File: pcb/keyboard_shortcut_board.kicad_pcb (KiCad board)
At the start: 2 copper layers, 96.4 x 90.9 mm, 34 parts, among them SW1 SW_Push, SW10 RotaryEncoder, SW2 SW_Push, SW3 SW_Push, SW4 SW_Push, SW5 SW_Push, SW6 SW_Push, SW7 SW_Push, SW8 SW_Push, SW9 SW_Push, U1 MOUDLE-SEEEDUINO-XIAO, U2 ER_OLEDM0.91_1x-I2C

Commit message: fix schematic power rails
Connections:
- net Net-(D1-VSS) renamed GND
- D1 pad 1: Net-(D1-VDD) -> +5V
- D2 pad 1: Net-(D1-VDD) -> +5V
- D3 pad 1: Net-(D1-VDD) -> +5V
- D4 pad 1: Net-(D1-VDD) -> +5V
- D5 pad 1: Net-(D1-VDD) -> +5V
- D6 pad 1: Net-(D1-VDD) -> +5V
- D7 pad 1: Net-(D1-VDD) -> +5V
- D8 pad 1: Net-(D1-VDD) -> +5V
- D9 pad 1: Net-(D1-VDD) -> +5V
- U1 pad 12: Net-(D1-VDD) -> unconnected-(U1-3V3-Pad12)
- U1 pad 14: Net-(U1-5V) -> +5V
- U2 pad 2: Net-(U1-5V) -> +5V
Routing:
- net +5V: track 0.00 -> 262.0 mm, vias 0 -> 4
- net Net-(D1-VDD): track 197.5 -> 0.00 mm, vias 3 -> 0
- net Net-(U1-5V): track 136.1 -> 0.00 mm, vias 7 -> 0
- net GND: track 257.2 -> 275.9 mm, vias 9 -> 16

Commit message: move XIAO 5mm right so USB-C clears the case wall
Receptacle sat 7.64mm inboard of the right board edge after the mounting
margin was added, too deep for a USB-C plug overmold to reach. Now 2.64mm.

Re-routed all 13 nets on the XIAO. Also repointed the SK6812 footprints at
the 3D model that actually ships with KiCad. DRC unchanged: 0 unconnected,
44 LED slot-clearance errors inherent to the supplied footprint.
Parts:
- moved U1 5.00 mm to (115.5, 94.7)
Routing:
- net Net-(U1-PA8_A4_D4_SDA): track 118.5 -> 108.8 mm, vias 4 -> 2
- net Net-(U1-PA9_A5_D5_SCL): track 113.9 -> 104.3 mm, vias 6 -> 2
- net Net-(U1-PA6_A10_D10_MOSI): track 61.7 -> 68.1 mm, vias 1 -> 0
- net Net-(U1-PA5_A9_D9_MISO): track 72.0 -> 65.7 mm, vias 4 -> 2
- net Net-(U1-PA7_A8_D8_SCK): track 55.2 -> 60.6 mm, vias 3 -> 1
- net Net-(D16-K): track 45.5 -> 40.9 mm
- net Net-(D1-DIN): track 70.4 -> 74.7 mm
- net Net-(U1-PB09_A7_D7_RX): track 62.2 -> 64.8 mm, vias 8 -> 5
- net +5V: track 262.0 -> 259.6 mm, vias 4 -> 18
- net Net-(D13-K): track 67.8 -> 69.9 mm
- net Net-(D10-K): track 80.2 -> 82.3 mm
- net Net-(U1-PA11_A3_D3): track 97.5 -> 99.6 mm, vias 4 -> 1
- net GND: track 275.9 -> 274.9 mm

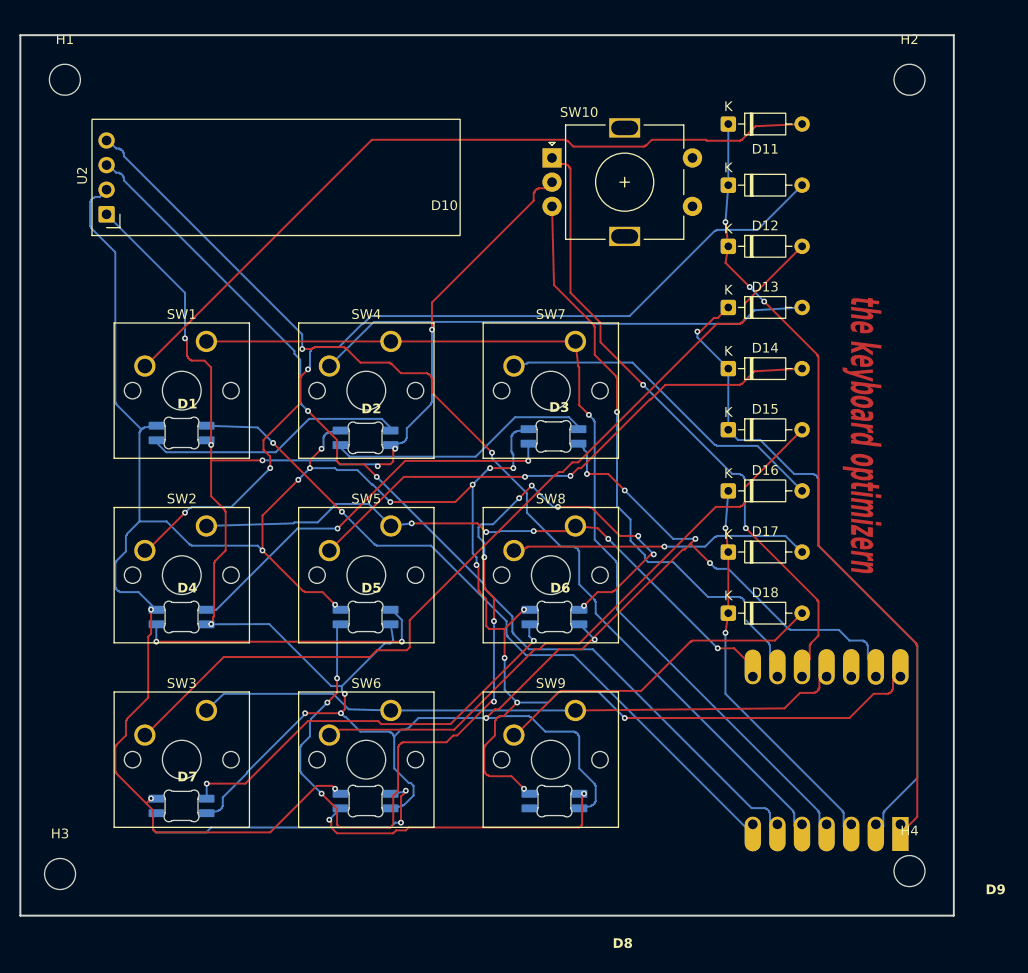
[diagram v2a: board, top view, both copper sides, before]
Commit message: square up the M3 mounting holes and add the board STEP
Holes were off a symmetric pattern by up to 0.7mm, so the case could not use
a rectangular pattern. Now a true 88.226 x 82.748 rectangle, 4.076mm inset on
all four edges.

That inset centres the bottom-right hole in the 8.15mm band between the XIAO
and the board edge, raising its clearance from 3.55 to 4.08mm so the heatset
boss can be 8.15mm OD instead of 7.1mm.

DRC unchanged: 0 unconnected, 44 LED slot-clearance errors from the supplied
SK6812 footprint. Gerbers and STEP regenerated and verified against the board.
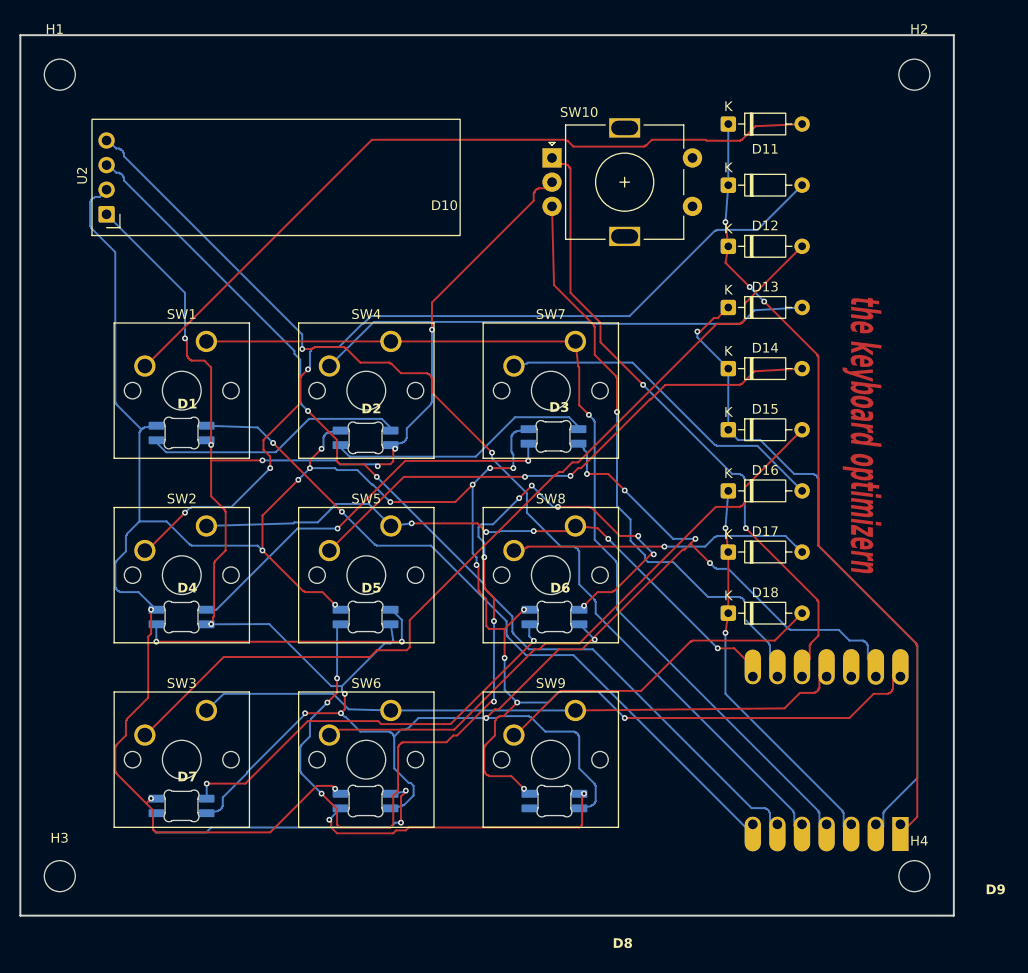
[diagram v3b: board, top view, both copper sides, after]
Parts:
- moved H1 0.74 mm to (36.3, 25.0)
- moved H2 0.73 mm to (124.5, 25.0)
- moved H4 0.73 mm to (124.5, 107.7)
- moved H3 0.23 mm to (36.3, 107.7)
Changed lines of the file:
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@@
 	(footprint "MountingHole:MountingHole_3.2mm_M3"
 		(layer "F.Cu")
-		(at 124.0172 25.4768)
+		(at 124.5186 24.9528)
 		(property "Reference" "H2"
-			(at 0 -4.15 0)
+			(at 0.5014 -4.6740 0)
 			(layer "F.SilkS")
 			(effects
@@
 		)
 		(property "Value" "MountingHole_3.2mm_M3"
-			(at 0 4.15 0)
+			(at 0.5014 3.6260 0)
 			(layer "F.Fab")
 			(effects
@@
 		)
 		(property "Datasheet" ""
-			(at 0 0 0)
+			(at 0.5014 -0.5240 0)
 			(layer "F.Fab")
 			(hide yes)
@@
 		)
 		(property "Description" ""
-			(at 0 0 0)
+			(at 0.5014 -0.5240 0)
 			(layer "F.Fab")
 			(hide yes)
@@
 		)
 		(property "KiLib_Generator" "mounting_hardware/mounting_hole"
-			(at 0 0 0)
+			(at 0.5014 -0.5240 0)
 			(layer "F.SilkS")
 			(hide yes)
@@
 		)
 		(fp_text user "${REFERENCE}"
-			(at 0 0 0)
+			(at 0.5014 -0.5240 0)
 			(layer "F.Fab")
 			(effects
@@
 	(footprint "MountingHole:MountingHole_3.2mm_M3"
 		(layer "F.Cu")
-		(at 124.0172 107.1768)
+		(at 124.5186 107.7007)
 		(property "Reference" "H4"
-			(at 0 -4.15 0)
+			(at 0.5014 -3.6261 0)
 			(layer "F.SilkS")
 			(effects
@@
 		)
 		(property "Value" "MountingHole_3.2mm_M3"
-			(at 0 4.15 0)
+			(at 0.5014 4.6739 0)
 			(layer "F.Fab")
 			(effects
@@
 		)
 		(property "Datasheet" ""
-			(at 0 0 0)
+			(at 0.5014 0.5239 0)
 			(layer "F.Fab")
 			(hide yes)
@@
 		)
 		(property "Description" ""
-			(at 0 0 0)
+			(at 0.5014 0.5239 0)
 			(layer "F.Fab")
 			(hide yes)
@@
 		)
 		(property "KiLib_Generator" "mounting_hardware/mounting_hole"
-			(at 0 0 0)
+			(at 0.5014 0.5239 0)
 			(layer "F.SilkS")
 			(hide yes)
@@
 		)
 		(fp_text user "${REFERENCE}"
-			(at 0 0 0)
+			(at 0.5014 0.5239 0)
 			(layer "F.Fab")
 			(effects
@@
 	(footprint "MountingHole:MountingHole_3.2mm_M3"
 		(layer "F.Cu")
-		(at 36.3172 107.4768)
+		(at 36.2932 107.7007)
 		(property "Reference" "H3"
-			(at 0 -4.15 0)
+			(at -0.0240 -3.9261 0)
 			(layer "F.SilkS")
 			(effects
@@
 		)
 		(property "Value" "MountingHole_3.2mm_M3"
-			(at 0 4.15 0)
+			(at -0.0240 4.3739 0)
 			(layer "F.Fab")
 			(effects
@@
 		)
 		(property "Datasheet" ""
-			(at 0 0 0)
+			(at -0.0240 0.2239 0)
 			(layer "F.Fab")
 			(hide yes)
@@
 		)
 		(property "Description" ""
-			(at 0 0 0)
+			(at -0.0240 0.2239 0)
 			(layer "F.Fab")
 			(hide yes)
@@
 		)
 		(property "KiLib_Generator" "mounting_hardware/mounting_hole"
-			(at 0 0 0)
+			(at -0.0240 0.2239 0)
 			(layer "F.SilkS")
 			(hide yes)
@@
 		)
 		(fp_text user "${REFERENCE}"
-			(at 0 0 0)
+			(at -0.0240 0.2239 0)
 			(layer "F.Fab")
 			(effects
@@
 	(footprint "MountingHole:MountingHole_3.2mm_M3"
 		(layer "F.Cu")
-		(at 36.8172 25.4768)
+		(at 36.2932 24.9528)
 		(property "Reference" "H1"
-			(at 0 -4.15 0)
+			(at -0.5240 -4.6740 0)
 			(layer "F.SilkS")
 			(effects
@@
 		)
 		(property "Value" "MountingHole_3.2mm_M3"
-			(at 0 4.15 0)
+			(at -0.5240 3.6260 0)
 			(layer "F.Fab")
 			(effects
@@
 		)
 		(property "Datasheet" ""
-			(at 0 0 0)
+			(at -0.5240 -0.5240 0)
 			(layer "F.Fab")
 			(hide yes)
@@
 		)
 		(property "Description" ""
-			(at 0 0 0)
+			(at -0.5240 -0.5240 0)
 			(layer "F.Fab")
 			(hide yes)
@@
 		)
 		(property "KiLib_Generator" "mounting_hardware/mounting_hole"
-			(at 0 0 0)
+			(at -0.5240 -0.5240 0)
 			(layer "F.SilkS")
 			(hide yes)
@@
 		)
 		(fp_text user "${REFERENCE}"
-			(at 0 0 0)
+			(at -0.5240 -0.5240 0)
 			(layer "F.Fab")
 			(effects
